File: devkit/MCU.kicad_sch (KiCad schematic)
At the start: 41 parts, among them IC601 FAN5622SX, IC602 USBLC6-2P6, IC603 MX25U51245GZ4I00, IC604 NTS0104GU12, J601 Jumper, J602 Jumper, J603 Jumper, J604 Jumper, M601 NORA-B106, X601 DEBUG, X602 Current, X603 Device, X604 UART, X605 GPIO, X606 Current, X607 IO Current, X608 Display, X609 Touch Current, X610 LED Current

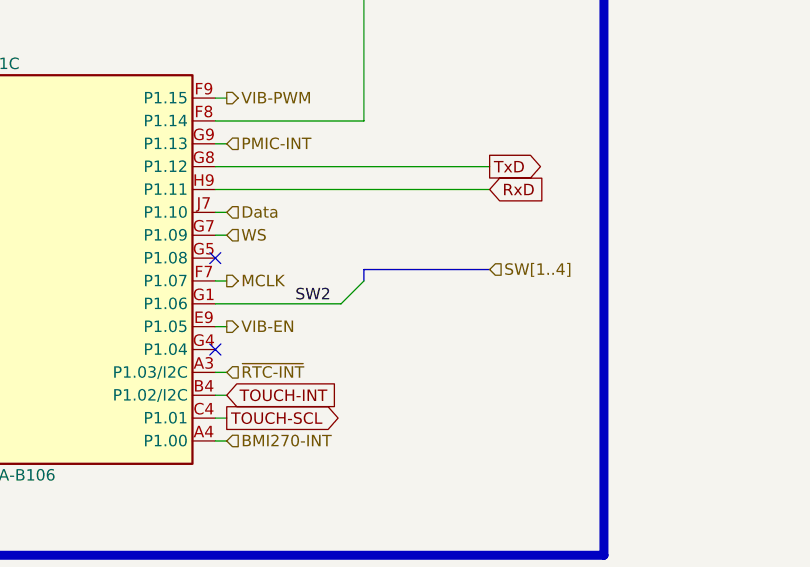
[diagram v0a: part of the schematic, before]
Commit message: Bug: Issue #155
The ship mode pin of the nPM1300 has an internal pull-up to VSYS.
Disconnect button 2 from the MCU and read it directly from the nPM1300.

Closes #155

Signed-off-by: Daniel Kampert <danielkampert@kampis-elektroecke.de>
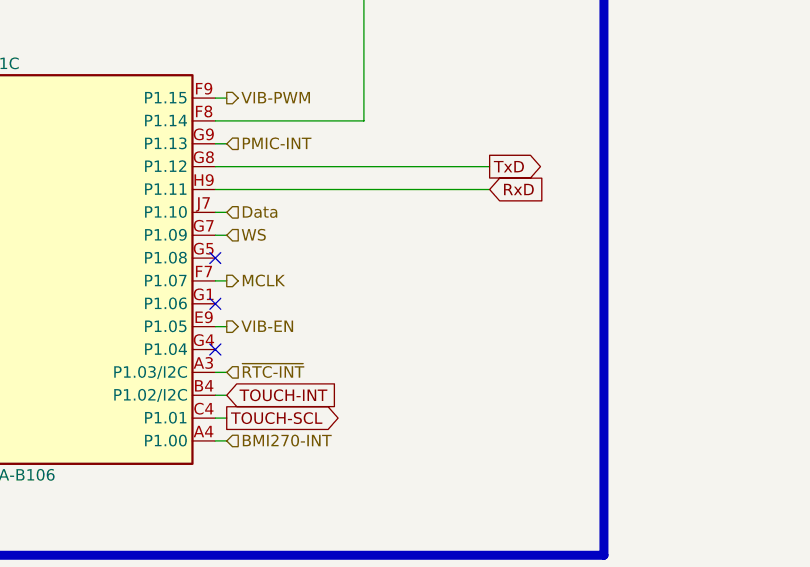
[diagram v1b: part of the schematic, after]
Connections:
- net SW2: no longer names the net of M601.G1 (P1.06)
- no-connect marks 12 -> 13
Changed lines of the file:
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@@
 	)
 	(no_connect
+		(at 231.14 127)
+	)
+	(no_connect
 		(at 153.67 69.85)
 	)
@@
 	)
 	(bus_entry
-		(at 247.65 124.46)
-		(size -2.54 2.54)
-		(stroke
-			(width 0)
-			(type default)
-		)
-	)
-	(bus_entry
 		(at 179.07 72.39)
 		(size -2.54 2.54)
@@
 		)
 	)
-	(bus
-		(pts
-			(xy 247.65 123.19) (xy 247.65 124.46)
-		)
-		(stroke
-			(width 0)
-			(type default)
-		)
-	)
 	(wire
 		(pts
@@
 	(wire
 		(pts
-			(xy 231.14 127) (xy 245.11 127)
-		)
-		(stroke
-			(width 0)
-			(type default)
-		)
-	)
-	(wire
-		(pts
 			(xy 59.69 69.85) (xy 60.96 69.85)
 		)
@@
 		)
 	)
-	(bus
-		(pts
-			(xy 261.62 123.19) (xy 247.65 123.19)
-		)
-		(stroke
-			(width 0)
-			(type default)
-		)
-	)
 	(polyline
 		(pts
@@
 		)
 	)
-	(label "SW2"
-		(at 240.03 127 0)
-		(effects
-			(font
-				(size 1.27 1.27)
-			)
-			(justify left bottom)
-		)
-	)
 	(label "SW3"
 		(at 170.18 80.01 0)
@@
 		(effects
 			(font
-				(size 1.27 1.27)
-			)
-			(justify left)
-		)
-	)
-	(hierarchical_label "SW[1..4]"
-		(shape input)
-		(at 261.62 123.19 0)
-		(effects
-			(font

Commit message: Task: Issue #157
- Change part number for SWD connector to 62201021121

Closes #157

Signed-off-by: Daniel Kampert <DanielKampert@kampis-elektroecke.de>
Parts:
- X601: manf# 62101021021 -> 62201021121; mouser# 710-62101021021 -> 710-62201021121
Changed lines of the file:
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@@
 			)
 		)
-		(property "manf#" "62101021021"
+		(property "manf#" "62201021121"
 			(at 41.91 255.27 0)
 			(effects
@@
 			)
 		)
-		(property "mouser#" "710-62101021021"
+		(property "mouser#" "710-62201021121"
 			(at 41.91 255.27 0)
 			(effects

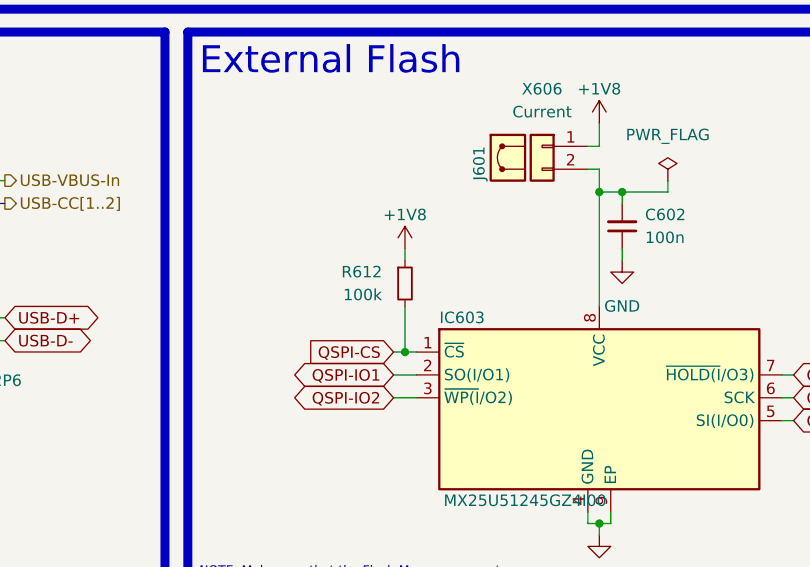
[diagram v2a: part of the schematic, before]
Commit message: Bug: Issue #158
- Fix silkscreens
- Add pull-up resistors to I2C lines
- Set the Pull-Up for Flash CS to NA
- Fix wrong part number for the I2C header

Closes #158

Signed-off-by: Daniel Kampert <DanielKampert@kampis-elektroecke.de>
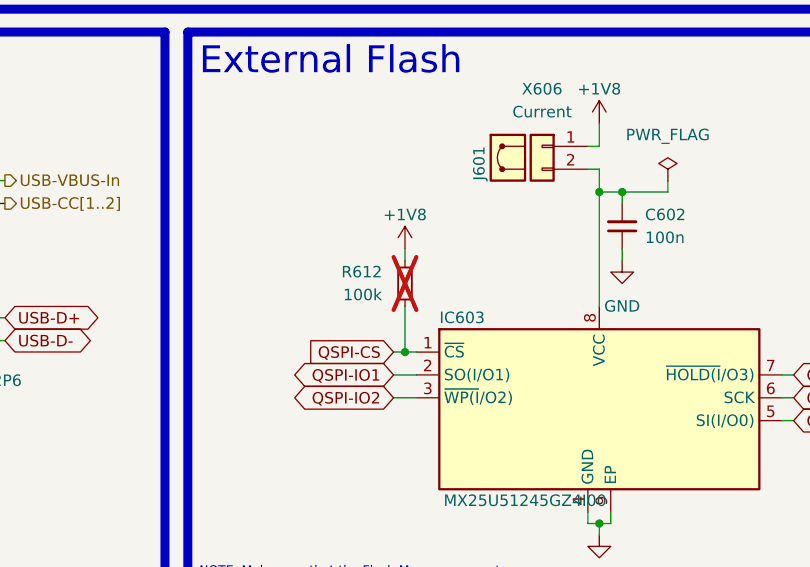
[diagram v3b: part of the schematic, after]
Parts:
- R612: now not fitted; now left out of the parts list
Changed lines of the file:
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@@
 		(dnp no)
 		(fields_autoplaced yes)
-		(property "Reference" "#PWR0616"
+		(property "Reference" "#PWR0615"
 			(at 215.9 185.42 0)
 			(effects
@@
 			(project "ZSWatch"
 				(path "/d5742f03-3b1a-42e5-a384-018bd4b919aa/c5103ceb-5325-4a84-a025-9638a412984e/8c9f2ee7-84da-4a9a-b0dc-117e0b0a9ea7"
-					(reference "#PWR0616")
+					(reference "#PWR0615")
 					(unit 1)
 				)
@@
 		(dnp no)
 		(fields_autoplaced yes)
-		(property "Reference" "#FLG0605"
+		(property "Reference" "#FLG0604"
 			(at 339.09 45.085 0)
 			(effects
@@
 			(project "ZSWatch-Watch-DevKit"
 				(path "/d5742f03-3b1a-42e5-a384-018bd4b919aa/c5103ceb-5325-4a84-a025-9638a412984e/8c9f2ee7-84da-4a9a-b0dc-117e0b0a9ea7"
-					(reference "#FLG0605")
+					(reference "#FLG0604")
 					(unit 1)
 				)
@@
 		(unit 1)
 		(exclude_from_sim no)
-		(in_bom yes)
+		(in_bom no)
 		(on_board yes)
-		(dnp no)
+		(dnp yes)
 		(fields_autoplaced yes)
 		(property "Reference" "R612"
@@
 		(dnp no)
 		(fields_autoplaced yes)
-		(property "Reference" "#FLG0602"
+		(property "Reference" "#FLG0601"
 			(at 60.96 175.895 0)
 			(effects
@@
 			(project "ZSWatch-Watch-DevKit"
 				(path "/d5742f03-3b1a-42e5-a384-018bd4b919aa/c5103ceb-5325-4a84-a025-9638a412984e/8c9f2ee7-84da-4a9a-b0dc-117e0b0a9ea7"
-					(reference "#FLG0602")
+					(reference "#FLG0601")
 					(unit 1)
 				)
@@
 		(dnp no)
 		(fields_autoplaced yes)
-		(property "Reference" "#FLG0601"
+		(property "Reference" "#FLG0602"
 			(at 67.31 66.675 0)
 			(effects
@@
 			(project "ZSWatch-Watch-DevKit"
 				(path "/d5742f03-3b1a-42e5-a384-018bd4b919aa/c5103ceb-5325-4a84-a025-9638a412984e/8c9f2ee7-84da-4a9a-b0dc-117e0b0a9ea7"
-					(reference "#FLG0601")
+					(reference "#FLG0602")
 					(unit 1)
 				)
@@
 		(dnp no)
 		(fields_autoplaced yes)
-		(property "Reference" "#FLG0604"
+		(property "Reference" "#FLG0605"
 			(at 367.03 47.625 0)
 			(effects
@@
 			(project "ZSWatch-Watch-DevKit"
 				(path "/d5742f03-3b1a-42e5-a384-018bd4b919aa/c5103ceb-5325-4a84-a025-9638a412984e/8c9f2ee7-84da-4a9a-b0dc-117e0b0a9ea7"
-					(reference "#FLG0604")
+					(reference "#FLG0605")
 					(unit 1)
 				)
@@
 		(on_board yes)
 		(dnp no)
-		(property "Reference" "#PWR0615"
+		(property "Reference" "#PWR0616"
 			(at 224.79 86.36 0)
 			(effects
@@
 			(project "Dev-Kit"
 				(path "/d5742f03-3b1a-42e5-a384-018bd4b919aa/c5103ceb-5325-4a84-a025-9638a412984e/8c9f2ee7-84da-4a9a-b0dc-117e0b0a9ea7"
-					(reference "#PWR0615")
+					(reference "#PWR0616")
 					(unit 1)
 				)

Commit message: Release 1.2.1
Signed-off-by: Daniel Kampert <DanielKampert@kampis-elektroecke.de>
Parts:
- R612: manf# RC0404FR-07100KL -> RC0402FR-07100KL; mouser# 603-RC0404FR-07100KL -> 603-RC0402FR-07100KL
- R613: manf Bourns -> YAGEO; manf# CR0805-J/-000ELF -> RC0805FR-07100KL; mouser# 652-CR0805-J/-000ELF -> 603-RC0805FR-07100KL
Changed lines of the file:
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@@
 			)
 		)
-		(property "manf#" "RC0404FR-07100KL"
+		(property "manf#" "RC0402FR-07100KL"
 			(at 215.9 185.42 0)
 			(effects
@@
 			)
 		)
-		(property "mouser#" "603-RC0404FR-07100KL"
+		(property "mouser#" "603-RC0402FR-07100KL"
 			(at 215.9 185.42 0)
 			(effects
@@
 			)
 		)
-		(property "Datasheet" "https://www.mouser.de/datasheet/3/40/1/cr.pdf"
+		(property "Datasheet" "https://www.mouser.com/catalog/specsheets/YAGEO_PYu_RC_Group_51_RoHS_L_12.pdf"
 			(at 331.47 48.26 0)
 			(effects
@@
 			)
 		)
-		(property "manf" "Bourns"
+		(property "manf" "YAGEO"
 			(at 331.47 48.26 0)
 			(effects
@@
 			)
 		)
-		(property "manf#" "CR0805-J/-000ELF"
+		(property "manf#" "RC0805FR-07100KL"
 			(at 331.47 48.26 0)
 			(effects
@@
 			)
 		)
-		(property "mouser#" "652-CR0805-J/-000ELF"
+		(property "mouser#" "603-RC0805FR-07100KL"
 			(at 331.47 48.26 0)
 			(effects

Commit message: Bug: Issue #165
Replace SWD connector with BD125-10-A-0305-0580-L-B

Closes #165

Signed-off-by: Daniel Kampert <danielkampert@kampis-elektroecke.de>
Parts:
- X601: manf Wurth Elektronik -> GCT; manf# 62201021121 -> BD125-10-A-0305-0580-L-B; mouser# 710-62201021121 -> 640-BD12510A305580LB
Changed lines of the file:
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@@
 			)
 		)
-		(property "Datasheet" "http://infocenter.arm.com/help/topic/com.arm.doc.ddi0314h/DDI0314H_coresight_components_trm.pdf"
+		(property "Datasheet" "https://gct.co/files/drawings/BD125.pdf"
 			(at 33.02 287.02 90)
 			(effects
@@
 			)
 		)
-		(property "manf" "Wurth Elektronik"
+		(property "manf" "GCT"
 			(at 41.91 255.27 0)
 			(effects
@@
 			)
 		)
-		(property "manf#" "62201021121"
+		(property "manf#" "BD125-10-A-0305-0580-L-B"
 			(at 41.91 255.27 0)
 			(effects
@@
 			)
 		)
-		(property "mouser#" "710-62201021121"
+		(property "mouser#" "640-BD12510A305580LB"
 			(at 41.91 255.27 0)
 			(effects

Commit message: Revert "Bug: Issue #165"
This reverts commit cfd33f8e9c92730593ade52965219aace560bf60.
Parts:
- X601: manf GCT -> Wurth Elektronik; manf# BD125-10-A-0305-0580-L-B -> 62201021121; mouser# 640-BD12510A305580LB -> 710-62201021121
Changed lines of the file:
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@@
 			)
 		)
-		(property "Datasheet" "https://gct.co/files/drawings/BD125.pdf"
+		(property "Datasheet" "http://infocenter.arm.com/help/topic/com.arm.doc.ddi0314h/DDI0314H_coresight_components_trm.pdf"
 			(at 33.02 287.02 90)
 			(effects
@@
 			)
 		)
-		(property "manf" "GCT"
+		(property "manf" "Wurth Elektronik"
 			(at 41.91 255.27 0)
 			(effects
@@
 			)
 		)
-		(property "manf#" "BD125-10-A-0305-0580-L-B"
+		(property "manf#" "62201021121"
 			(at 41.91 255.27 0)
 			(effects
@@
 			)
 		)
-		(property "mouser#" "640-BD12510A305580LB"
+		(property "mouser#" "710-62201021121"
 			(at 41.91 255.27 0)
 			(effects
